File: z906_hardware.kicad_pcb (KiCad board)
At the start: 2 copper layers, 11 parts, among them J1 USB_C_Receptacle_USB2.0_14P, U1 ESP32-S3-WROOM-1, U2 AP63203WU, U3 PCM5102A, U4 TPD2EUSB30, U5 TPD1E05U06DYA, U6 TPS7A4533, U7 PCM1860DBT, U8 TPD2E2U06DCK

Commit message: add footprint
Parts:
- removed U8: TPD2E2U06DCK, Package_TO_SOT_SMD:SOT-323_SC-70
- added C10: 22uF, Capacitor_SMD:C_0805_2012Metric_Pad1.18x1.45mm_HandSolder, F.Cu at (50.9, 58.1)
- added C11: 1uF, Capacitor_SMD:C_0805_2012Metric_Pad1.18x1.45mm_HandSolder, F.Cu at (50.9, 61.1)
- added C12: 100nF, Capacitor_SMD:C_0805_2012Metric_Pad1.18x1.45mm_HandSolder, F.Cu at (50.9, 64.1)
- added C13: 100nF, Capacitor_SMD:C_0805_2012Metric_Pad1.18x1.45mm_HandSolder, F.Cu at (55.7, 40.0)
- added C14: 10uF, Capacitor_SMD:C_0805_2012Metric_Pad1.18x1.45mm_HandSolder, F.Cu at (55.7, 43.0)
- added C15: 0.1uF, Capacitor_SMD:C_0805_2012Metric_Pad1.18x1.45mm_HandSolder, F.Cu at (55.7, 46.0)
- added C16: 10uF, Capacitor_SMD:C_0805_2012Metric_Pad1.18x1.45mm_HandSolder, F.Cu at (55.7, 49.0)
- added C17: 0.1uF, Capacitor_SMD:C_0805_2012Metric_Pad1.18x1.45mm_HandSolder, F.Cu at (55.7, 52.0)
- added C18: 10uF, Capacitor_SMD:C_0805_2012Metric_Pad1.18x1.45mm_HandSolder, F.Cu at (55.7, 55.1)
- added C19: 0.1uF, Capacitor_SMD:C_0805_2012Metric_Pad1.18x1.45mm_HandSolder, F.Cu at (55.7, 58.1)
- added C2: 10uF, Capacitor_SMD:C_0805_2012Metric_Pad1.18x1.45mm_HandSolder, F.Cu at (50.9, 40.0)
- added C20: 0.1uF, Capacitor_SMD:C_0805_2012Metric_Pad1.18x1.45mm_HandSolder, F.Cu at (55.7, 61.1)
- added C21: 10uF, Capacitor_SMD:C_0805_2012Metric_Pad1.18x1.45mm_HandSolder, F.Cu at (55.7, 64.1)
- added C22: 2.2uF, Capacitor_SMD:C_0805_2012Metric_Pad1.18x1.45mm_HandSolder, F.Cu at (60.5, 40.0)
- added C23: 2.2uF, Capacitor_SMD:C_0805_2012Metric_Pad1.18x1.45mm_HandSolder, F.Cu at (60.5, 43.0)
- added C24: 2.2nF, Capacitor_SMD:C_0805_2012Metric_Pad1.18x1.45mm_HandSolder, F.Cu at (60.5, 46.0)
- added C25: 2.2nF, Capacitor_SMD:C_0805_2012Metric_Pad1.18x1.45mm_HandSolder, F.Cu at (60.5, 49.0)
- added C26: 10uF, Capacitor_SMD:C_0805_2012Metric_Pad1.18x1.45mm_HandSolder, F.Cu at (60.5, 52.0)
- added C27: 0.1uF, Capacitor_SMD:C_0805_2012Metric_Pad1.18x1.45mm_HandSolder, F.Cu at (60.5, 55.1)
- added C28: 10uF, Capacitor_SMD:C_0805_2012Metric_Pad1.18x1.45mm_HandSolder, F.Cu at (60.5, 58.1)
- added C29: 0.1uF, Capacitor_SMD:C_0805_2012Metric_Pad1.18x1.45mm_HandSolder, F.Cu at (60.5, 61.1)
- added C30: 10uF, Capacitor_SMD:C_0805_2012Metric_Pad1.18x1.45mm_HandSolder, F.Cu at (60.5, 64.1)
- added C31: 0.1uF, Capacitor_SMD:C_0805_2012Metric_Pad1.18x1.45mm_HandSolder, F.Cu at (65.3, 40.0)
- added C32: 10uF, Capacitor_SMD:C_0805_2012Metric_Pad1.18x1.45mm_HandSolder, F.Cu at (65.3, 43.0)
- added C33: 0.1uF, Capacitor_SMD:C_0805_2012Metric_Pad1.18x1.45mm_HandSolder, F.Cu at (65.3, 46.0)
- added C34: 2.2uF, Capacitor_SMD:C_0805_2012Metric_Pad1.18x1.45mm_HandSolder, F.Cu at (65.3, 49.0)
- added C35: 4.7uF, Capacitor_SMD:C_1206_3216Metric_Pad1.33x1.80mm_HandSolder, F.Cu at (70.7, 63.8)
- added C36: 1nF, Capacitor_SMD:C_0603_1608Metric_Pad1.08x0.95mm_HandSolder, F.Cu at (81.5, 63.4)
- added C37: 4.7uF, Capacitor_SMD:C_1206_3216Metric_Pad1.33x1.80mm_HandSolder, F.Cu at (70.7, 67.1)
- added C38: 1nF, Capacitor_SMD:C_0603_1608Metric_Pad1.08x0.95mm_HandSolder, F.Cu at (81.5, 65.9)
- added C39: 100nF, Capacitor_SMD:C_0805_2012Metric_Pad1.18x1.45mm_HandSolder, F.Cu at (65.3, 52.0)
- added C4: 22uF, Capacitor_SMD:C_0805_2012Metric_Pad1.18x1.45mm_HandSolder, F.Cu at (50.9, 43.0)
- added C6: 10uF, Capacitor_SMD:C_0805_2012Metric_Pad1.18x1.45mm_HandSolder, F.Cu at (50.9, 46.0)
- added C7: 10uF, Capacitor_SMD:C_0805_2012Metric_Pad1.18x1.45mm_HandSolder, F.Cu at (50.9, 49.0)
- added C8: 0.1uF, Capacitor_SMD:C_0805_2012Metric_Pad1.18x1.45mm_HandSolder, F.Cu at (50.9, 52.0)
- added C9: 0.1uF, Capacitor_SMD:C_0805_2012Metric_Pad1.18x1.45mm_HandSolder, F.Cu at (50.9, 55.1)
- added F1: 0ZLM0075FF2G, Fuse:Fuse_0603_1608Metric_Pad1.05x0.95mm_HandSolder, F.Cu at (102.0, 66.5)
- added J5: Ampli, Connector_TE-Connectivity:TE_Micro-MaTch_1-215079-6_2x08_P1.27mm_Vertical, F.Cu at (172.0, 99.2)
- added J6: Console, Connector_Dsub:DSUB-15-HD_Pins_Horizontal_P2.29x1.90mm_EdgePinOffset3.03mm_Housed_MountingHolesOffset4.94mm, F.Cu at (91.8, 108.0)
- added L1: 1.0uH, Inductor_SMD:L_1008_2520Metric_Pad1.43x2.20mm_HandSolder, F.Cu at (71.0, 81.0)
- added R1: 5.1k, Resistor_SMD:R_0805_2012Metric_Pad1.20x1.40mm_HandSolder, F.Cu at (102.0, 74.0)
- added R10: 100k, Resistor_SMD:R_0805_2012Metric_Pad1.20x1.40mm_HandSolder, F.Cu at (74.9, 42.9)
- added R11: 100k, Resistor_SMD:R_0805_2012Metric_Pad1.20x1.40mm_HandSolder, F.Cu at (74.9, 45.9)
- added R12: 100, Resistor_SMD:R_0805_2012Metric_Pad1.20x1.40mm_HandSolder, F.Cu at (74.9, 48.8)
- added R13: 1k, Resistor_SMD:R_0805_2012Metric_Pad1.20x1.40mm_HandSolder, F.Cu at (74.9, 51.8)
- added R14: 22, Resistor_SMD:R_0805_2012Metric_Pad1.20x1.40mm_HandSolder, F.Cu at (74.9, 54.7)
- added R15: 22, Resistor_SMD:R_0805_2012Metric_Pad1.20x1.40mm_HandSolder, F.Cu at (74.9, 57.7)
- added R16: 0, Resistor_SMD:R_0805_2012Metric_Pad1.20x1.40mm_HandSolder, F.Cu at (74.9, 60.6)
- added R17: 0, Resistor_SMD:R_0805_2012Metric_Pad1.20x1.40mm_HandSolder, F.Cu at (79.6, 40.0)
- added R18: 0, Resistor_SMD:R_0805_2012Metric_Pad1.20x1.40mm_HandSolder, F.Cu at (79.6, 42.9)
- added R19: 0, Resistor_SMD:R_0805_2012Metric_Pad1.20x1.40mm_HandSolder, F.Cu at (79.6, 45.9)
- added R2: 5.1k, Resistor_SMD:R_0805_2012Metric_Pad1.20x1.40mm_HandSolder, F.Cu at (102.0, 68.5)
- added R20: 0, Resistor_SMD:R_0805_2012Metric_Pad1.20x1.40mm_HandSolder, F.Cu at (79.6, 48.8)
- added R21: 0, Resistor_SMD:R_0805_2012Metric_Pad1.20x1.40mm_HandSolder, F.Cu at (79.6, 51.8)
- added R22: 0, Resistor_SMD:R_0805_2012Metric_Pad1.20x1.40mm_HandSolder, F.Cu at (79.6, 54.7)
- added R23: 0, Resistor_SMD:R_0805_2012Metric_Pad1.20x1.40mm_HandSolder, F.Cu at (79.6, 57.7)
- added R24: 0, Resistor_SMD:R_0805_2012Metric_Pad1.20x1.40mm_HandSolder, F.Cu at (79.6, 60.6)
- added R25: 0, Resistor_SMD:R_0805_2012Metric_Pad1.20x1.40mm_HandSolder, F.Cu at (84.4, 40.0)
- added R26: 10, Resistor_SMD:R_1206_3216Metric, F.Cu at (76.6, 63.8)
- added R27: 10k, Resistor_SMD:R_0805_2012Metric_Pad1.20x1.40mm_HandSolder, F.Cu at (84.4, 42.9)
- added R28: 10k, Resistor_SMD:R_0805_2012Metric_Pad1.20x1.40mm_HandSolder, F.Cu at (84.4, 45.9)
- added R29: 10k, Resistor_SMD:R_0805_2012Metric_Pad1.20x1.40mm_HandSolder, F.Cu at (84.4, 48.8)
- added R3: 453k, Resistor_SMD:R_0805_2012Metric_Pad1.20x1.40mm_HandSolder, F.Cu at (70.1, 45.9)
- added R4: 0, Resistor_SMD:R_0805_2012Metric_Pad1.20x1.40mm_HandSolder, F.Cu at (70.1, 48.8)
- added R5: 10K, Resistor_SMD:R_0805_2012Metric_Pad1.20x1.40mm_HandSolder, F.Cu at (70.1, 51.8)
- added R6: 470, Resistor_SMD:R_0805_2012Metric_Pad1.20x1.40mm_HandSolder, F.Cu at (70.1, 54.7)
- added R7: 470, Resistor_SMD:R_0805_2012Metric_Pad1.20x1.40mm_HandSolder, F.Cu at (70.1, 57.7)
- added R8: 100k, Resistor_SMD:R_0805_2012Metric_Pad1.20x1.40mm_HandSolder, F.Cu at (70.1, 60.6)
- added R9: 100, Resistor_SMD:R_0805_2012Metric_Pad1.20x1.40mm_HandSolder, F.Cu at (74.9, 40.0)
- added TP2: RXD0, Connector_Pin:Pin_D1.0mm_L10.0mm, F.Cu at (161.5, 72.0)
- added TP3: TXD0, Connector_Pin:Pin_D1.0mm_L10.0mm, F.Cu at (161.5, 68.0)
- added TP4: 3.3VA, Connector_Pin:Pin_D1.0mm_L10.0mm, F.Cu at (109.0, 100.0)
- added TP5: GND, Connector_Pin:Pin_D1.0mm_L10.0mm, F.Cu at (122.5, 78.0)
- added TP6: 3.3V, Connector_Pin:Pin_D1.0mm_L10.0mm, F.Cu at (112.5, 40.5)
- JP1: value jumper -> reset
- JP2: value jumper -> boot
- U2: value AP63203WU -> TPS62A02APDDC; footprint Package_TO_SOT_SMD:TSOT-23-6 -> Package_TO_SOT_SMD:SOT-23-6
- U6: footprint Package_TO_SOT_SMD:TO-263-5_TabPin3 -> Package_TO_SOT_SMD:SOT-223-6_TabPin3
- moved U7 71.0 mm to (115.9, 100.0)
- moved U1 45.4 mm to (145.1, 72.5)
- moved U2 42.3 mm to (118.5, 39.5)
- moved U5 39.8 mm to (105.0, 67.0), turned to -90 degrees
- moved JP1 38.8 mm to (129.2, 70.5), turned to 0 degrees
- moved JP2 38.3 mm to (129.8, 77.5), turned to 0 degrees
- moved U4 36.4 mm to (102.0, 71.0)
- moved J1 33.2 mm to (94.0, 70.5)
- moved U6 28.9 mm to (113.5, 79.5), turned to 0 degrees
- moved U3 25.1 mm to (147.6, 101.3)
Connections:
- net /chip_pu renamed Net-(JP1-B)
- J1 pad A4: +5V -> Net-(F1-Pad1)
- J1 pad A6: /USB_DP -> Net-(U4-D+)
- J1 pad A7: /USB_DN -> Net-(U4-D-)
- J1 pad A9: +5V -> Net-(F1-Pad1)
- J1 pad B4: +5V -> Net-(F1-Pad1)
- J1 pad B6: /USB_DP -> Net-(U4-D+)
- J1 pad B7: /USB_DN -> Net-(U4-D-)
- J1 pad B9: +5V -> Net-(F1-Pad1)
- JP2 pad 2: /GPIO0 -> Net-(JP2-B)
- U1 pad 10: /tx_amplifier -> Net-(U1-IO17)
- U1 pad 11: /rx_amplifier -> Net-(U1-IO18)
- U1 pad 12: /console_powered -> Net-(U1-IO8)
- U1 pad 13: /USB_DN -> Net-(U1-USB_D-)
- U1 pad 14: /USB_DP -> Net-(U1-USB_D+)
- U1 pad 17: /console_presence -> Net-(U1-IO9)
- U1 pad 18: /DAC_DATA -> Net-(U1-IO10)
- U1 pad 19: /MCLK -> unconnected-(U1-IO11-Pad19)
- U1 pad 27: /GPIO0 -> Net-(U1-IO0)
- U1 pad 31: unconnected-(U1-IO38-Pad31) -> /DAC_DATA
- U1 pad 36: unconnected-(U1-RXD0-Pad36) -> Net-(U1-RXD0)
- U1 pad 37: unconnected-(U1-TXD0-Pad37) -> Net-(U1-TXD0)
- U1 pad 4: /amplifier_presence -> /BCK
- U1 pad 5: /LCK -> Net-(U1-IO5)
- U1 pad 6: /BCK -> /ADC_DATA
- U1 pad 7: /ADC_DATA -> Net-(U1-IO7)
- U1 pad 8: /rx_console -> Net-(U1-IO15)
- U1 pad 9: /tx_console -> Net-(U1-IO16)
- U2 pad 1: +3.3V -> Net-(U2-EN)
- U2 pad 2: +5V -> GND
- U2 pad 3: +5V -> Net-(U2-SW)
- U2 pad 4: GND -> Net-(U2-EN)
- U2 pad 5: Net-(U2-SW) -> unconnected-(U2-PG-Pad5)
- U3 pad 15: /LCK -> /BCK
- U4 pad 1: /USB_DP -> Net-(U4-D+)
- U4 pad 2: /USB_DN -> Net-(U4-D-)
- U5 pad 1: +5V -> Net-(U2-EN)
- U7 pad 16: /LCK -> /BCK
- U7 pad 19: Net-(U7-INT) -> unconnected-(U7-INT-Pad19)
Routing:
- net Net-(U4-D-): track 0.00 -> 6.28 mm
- net Net-(F1-Pad1): track 0.00 -> 4.11 mm
- net Net-(U4-D+): track 0.00 -> 4.04 mm
- net Net-(J1-CC1): track 0.00 -> 3.63 mm
- net Net-(U2-EN): track 0.00 -> 2.21 mm

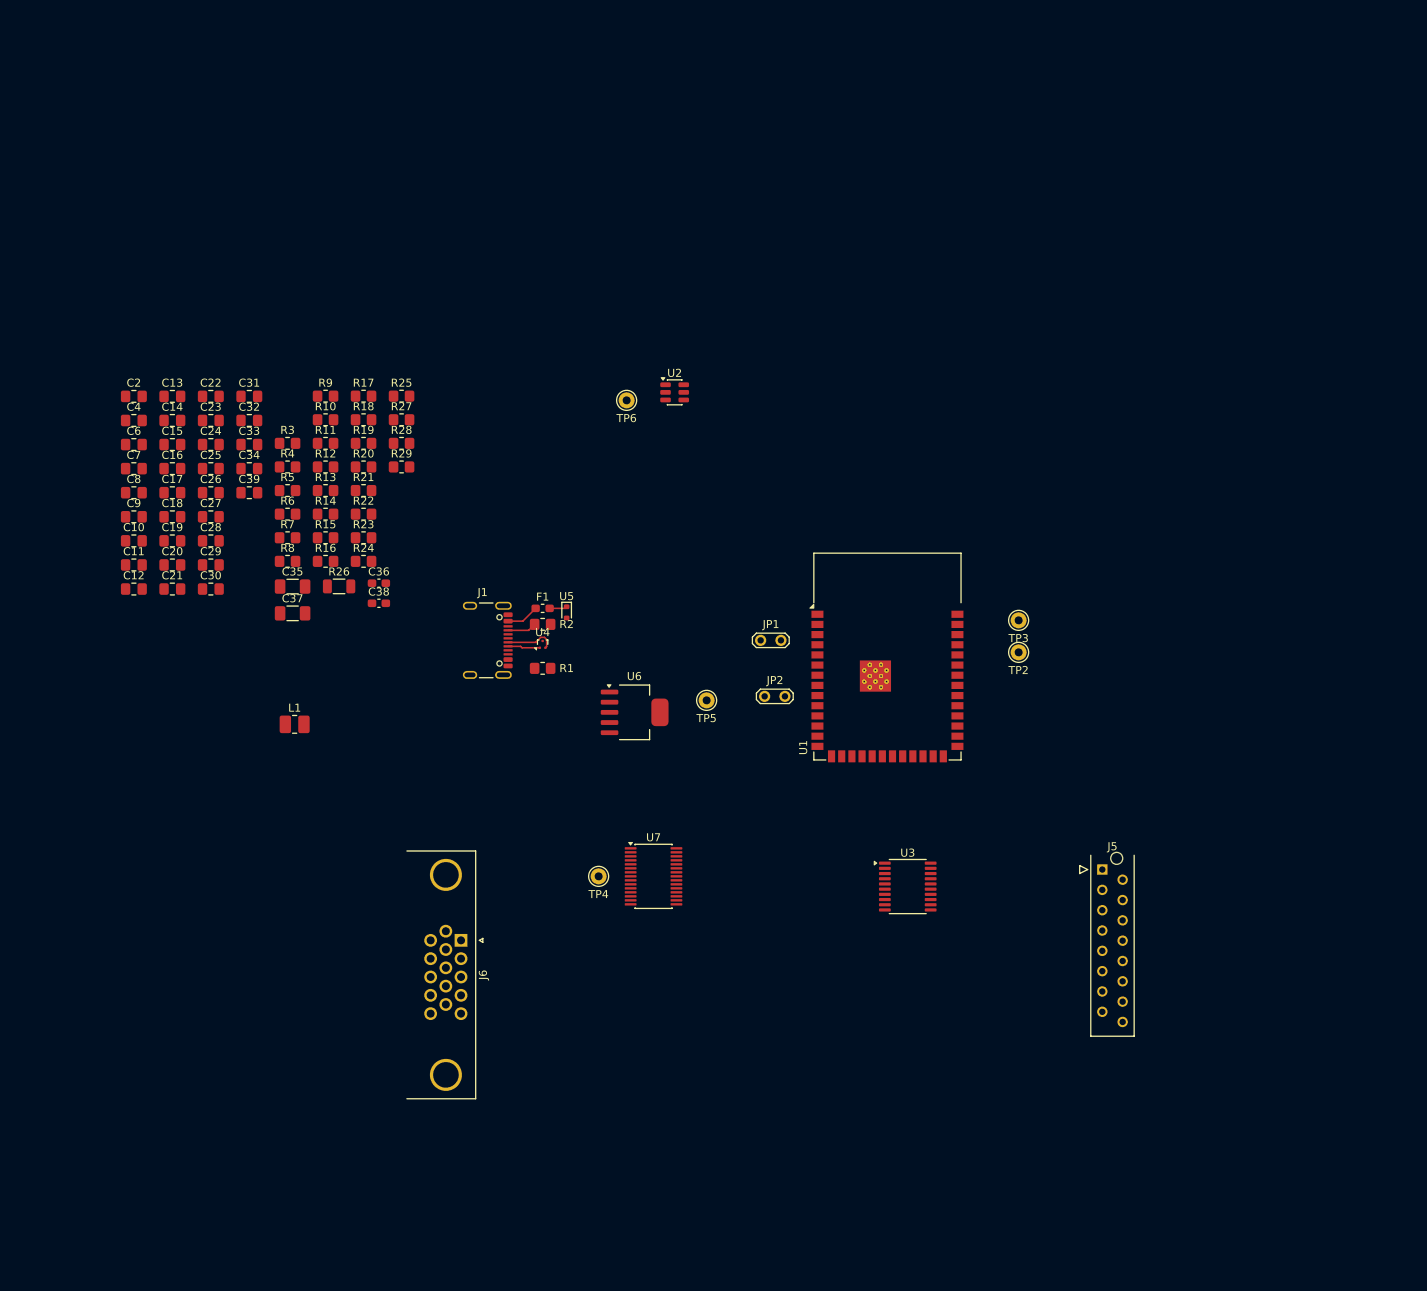
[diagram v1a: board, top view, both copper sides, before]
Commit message: start placing composants
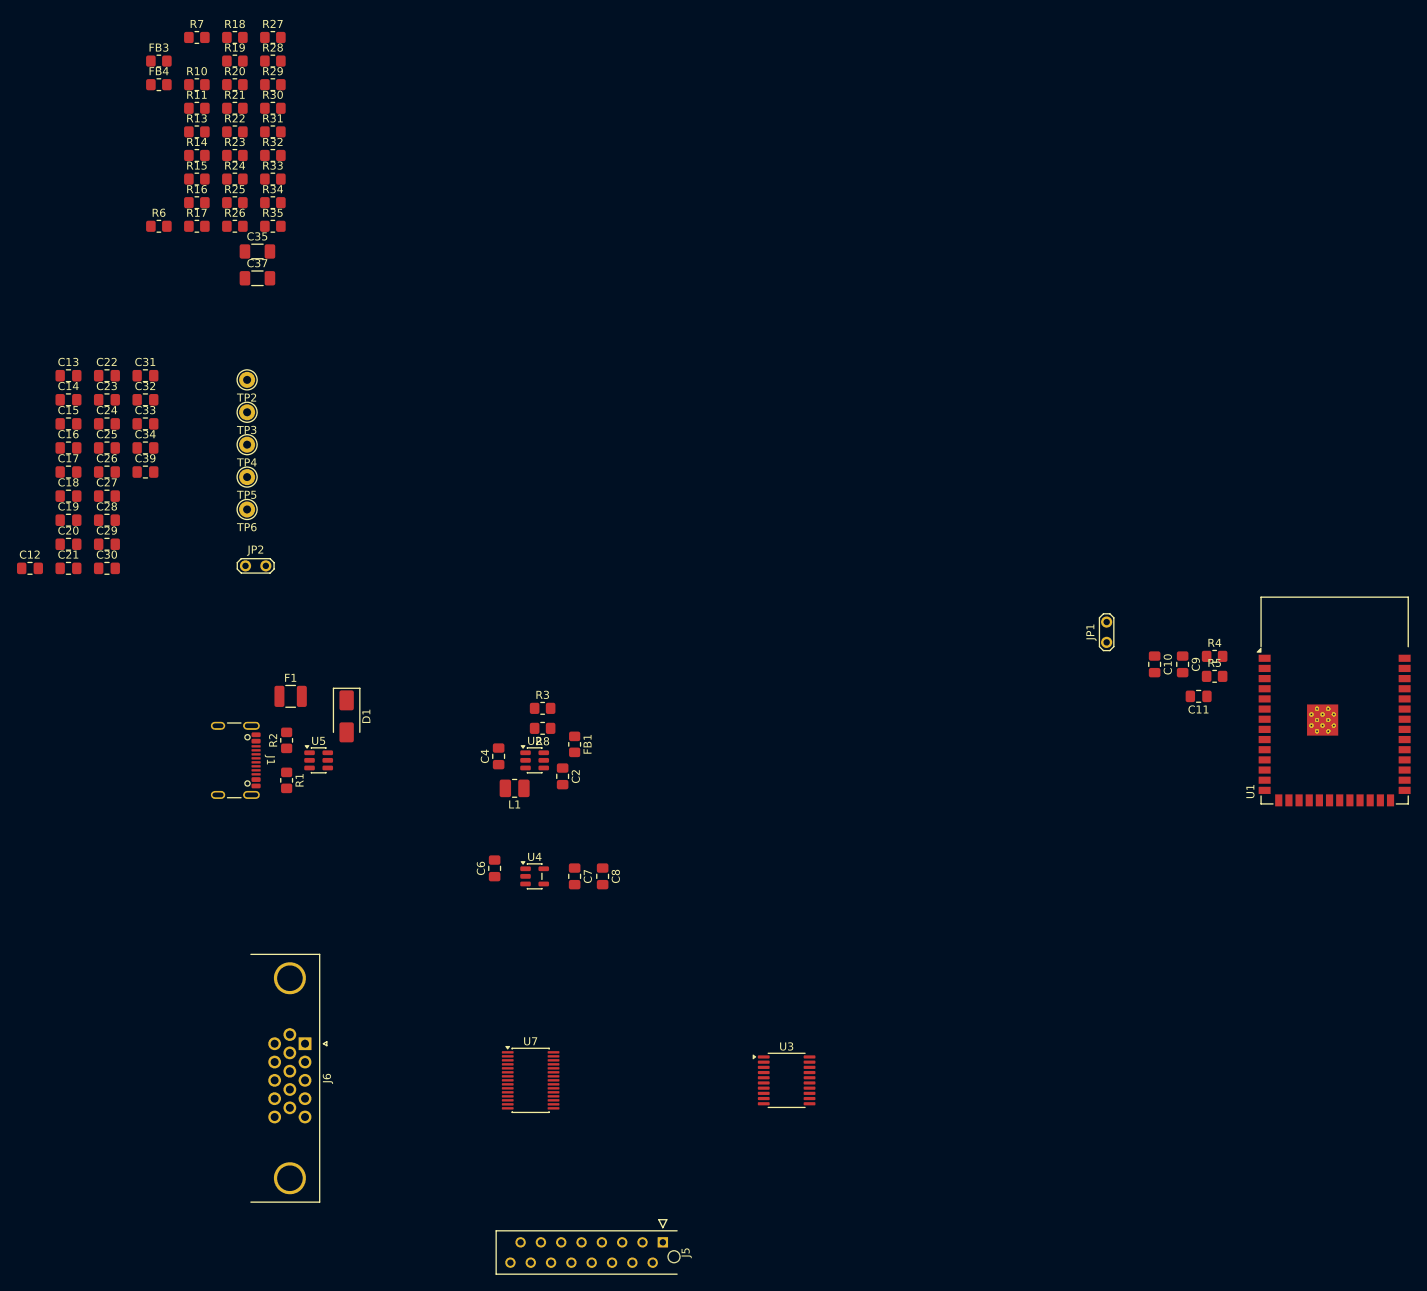
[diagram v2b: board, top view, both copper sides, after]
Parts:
- removed C36, C38: 1nF, Capacitor_SMD:C_0603_1608Metric_Pad1.08x0.95mm_HandSolder
- removed R12, R9: 100, Resistor_SMD:R_0805_2012Metric_Pad1.20x1.40mm_HandSolder
- removed U6: TPS7A4533, Package_TO_SOT_SMD:SOT-223-6_TabPin3
- added D1: SMAJ5.0A, Diode_SMD:D_SMA, F.Cu at (77.5, 80.0)
- added FB1: 600Ohm@100MHz, Resistor_SMD:R_0805_2012Metric_Pad1.20x1.40mm_HandSolder, F.Cu at (106.0, 83.5)
- added FB3: 600Ohm@100MHz, Resistor_SMD:R_0805_2012Metric_Pad1.20x1.40mm_HandSolder, F.Cu at (54.0, -1.91)
- added FB4: 600Ohm@100MHz, Resistor_SMD:R_0805_2012Metric_Pad1.20x1.40mm_HandSolder, F.Cu at (54.0, 1.04)
- added R30: 0, Resistor_SMD:R_0805_2012Metric_Pad1.20x1.40mm_HandSolder, F.Cu at (68.3, 3.99)
- added R31: 22, Resistor_SMD:R_0805_2012Metric_Pad1.20x1.40mm_HandSolder, F.Cu at (68.3, 6.94)
- added R32: 22, Resistor_SMD:R_0805_2012Metric_Pad1.20x1.40mm_HandSolder, F.Cu at (68.3, 9.89)
- added R33: 22, Resistor_SMD:R_0805_2012Metric_Pad1.20x1.40mm_HandSolder, F.Cu at (68.3, 12.8)
- added R34: 0, Resistor_SMD:R_0805_2012Metric_Pad1.20x1.40mm_HandSolder, F.Cu at (68.3, 15.8)
- added R35: 10k, Resistor_SMD:R_0805_2012Metric_Pad1.20x1.40mm_HandSolder, F.Cu at (68.3, 18.7)
- C11: value 1uF -> 2.2uF
- C15, C17, C19, C20, C27, C29, C31, C33, C8, C9: value 0.1uF -> 100nF
- C35, C37: value 4.7uF -> 10uF
- F1: value 0ZLM0075FF2G -> 0ZCJ0075AF2E; footprint Fuse:Fuse_0603_1608Metric_Pad1.05x0.95mm_HandSolder -> Fuse:Fuse_1210_3225Metric
- J1: value USB_C_Receptacle_USB2.0_14P -> USB_C_Receptacle_USB2.0_16P
- R16, R17, R18, R19: value 0 -> 1k
- R26: value 10 -> 0; footprint Resistor_SMD:R_1206_3216Metric -> Resistor_SMD:R_0805_2012Metric_Pad1.20x1.40mm_HandSolder
- R5: value 10K -> 10k
- U4: value TPD2EUSB30 -> TPS7A2033PDBVR; footprint Package_TO_SOT_SMD:Texas_DRT-3 -> Package_TO_SOT_SMD:SOT-23-5
- U5: value TPD1E05U06DYA -> USBLC6-2SC6; footprint Diode_SMD:D_SOD-523 -> Package_TO_SOT_SMD:SOT-23-6
- moved C11 134.1 mm to (184.0, 77.5), turned to 180 degrees
- moved C9 132.4 mm to (182.0, 73.5), turned to -90 degrees
- moved C10 128.5 mm to (178.5, 73.5), turned to -90 degrees
- moved R4 118.3 mm to (186.0, 72.5)
- moved R5 118.2 mm to (186.0, 75.0)
- moved TP2 102.3 mm to (65.1, 37.9)
- moved TP3 99.9 mm to (65.1, 42.0)
- moved C8 75.7 mm to (109.5, 100.0), turned to -90 degrees
- moved C7 75.1 mm to (106.0, 100.0), turned to -90 degrees
- moved J5 72.0 mm to (117.0, 145.7), turned to -90 degrees
- moved C2 71.6 mm to (104.5, 87.5), turned to -90 degrees
- moved TP4 69.6 mm to (65.1, 46.0)
- moved C6 69.6 mm to (96.0, 99.0), turned to 90 degrees
- moved JP2 66.9 mm to (64.9, 61.2)
- moved TP5 63.9 mm to (65.1, 50.1)
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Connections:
- net /MCLK renamed /I2S.MCLK
- C14 pad 1: +3.3VA -> Net-(U3-AVDD)
- C15 pad 1: +3.3VA -> Net-(U3-AVDD)
- C18 pad 1: +3.3VA -> Net-(U3-CPVDD)
- C19 pad 1: +3.3VA -> Net-(U3-CPVDD)
- C30 pad 1: +3.3VA -> Net-(U7-AVDD)
- C31 pad 1: +3.3VA -> Net-(U7-AVDD)
- C35 pad 2: Net-(C35-Pad2) -> Net-(U7-VINL1/VIN1P)
- C37 pad 2: Net-(C37-Pad2) -> Net-(U7-VINR1/VIN2P)
- C6 pad 1: Net-(U6-IN) -> Net-(D1-K)
- F1 pad 2: Net-(U2-EN) -> Net-(D1-K)
- J1 pad A6: Net-(U4-D+) -> Net-(J1-D+-PadA6)
- J1 pad A7: Net-(U4-D-) -> Net-(J1-D--PadA7)
- J1 pad A8: (no net) -> unconnected-(J1-SBU1-PadA8)
- J1 pad B6: Net-(U4-D+) -> Net-(J1-D+-PadA6)
- J1 pad B7: Net-(U4-D-) -> Net-(J1-D--PadA7)
- J1 pad B8: (no net) -> unconnected-(J1-SBU2-PadB8)
- R14 pad 1: /BCK -> /I2S.LCK
- R20 pad 2: Net-(U4-D-) -> Net-(R20-Pad2)
- R21 pad 2: Net-(U4-D+) -> Net-(R21-Pad2)
- R26 pad 1: Net-(U6-IN) -> Net-(J5-Pin_12)
- R26 pad 2: Net-(U2-EN) -> Net-(J6-Pin_12)
- U1 pad 31: /DAC_DATA -> Net-(U1-IO38)
- U1 pad 32: unconnected-(U1-IO39-Pad32) -> Net-(U1-IO39)
- U1 pad 4: /BCK -> Net-(U1-IO4)
- U1 pad 6: /ADC_DATA -> Net-(U1-IO6)
- U3 pad 1: +3.3VA -> Net-(U3-CPVDD)
- U3 pad 13: /BCK -> /I2S.BCK
- U3 pad 14: /DAC_DATA -> /I2S.DAC
- U3 pad 15: /BCK -> /I2S.LCK
- U3 pad 17: +3.3V -> Net-(U1-IO39)
- U3 pad 8: +3.3VA -> Net-(U3-AVDD)
- U4 pad 1: Net-(U4-D+) -> Net-(D1-K)
- U4 pad 2: Net-(U4-D-) -> GND
- U4 pad 3: GND -> Net-(D1-K)
- U5 pad 1: Net-(U2-EN) -> Net-(J1-D--PadA7)
- U7 pad 16: /BCK -> /I2S.LCK
- U7 pad 17: /BCK -> /I2S.BCK
- U7 pad 18: /ADC_DATA -> /I2S.ADC
- U7 pad 8: +3.3VA -> Net-(U7-AVDD)
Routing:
- net Net-(U4-D-): track 6.28 -> 0.00 mm
- net Net-(F1-Pad1): track 4.11 -> 0.00 mm
- net Net-(U4-D+): track 4.04 -> 0.00 mm
- net Net-(J1-CC1): track 3.63 -> 0.00 mm
- net Net-(U2-EN): track 2.21 -> 0.00 mm
